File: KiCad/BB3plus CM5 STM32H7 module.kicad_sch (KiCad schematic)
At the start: 9 parts

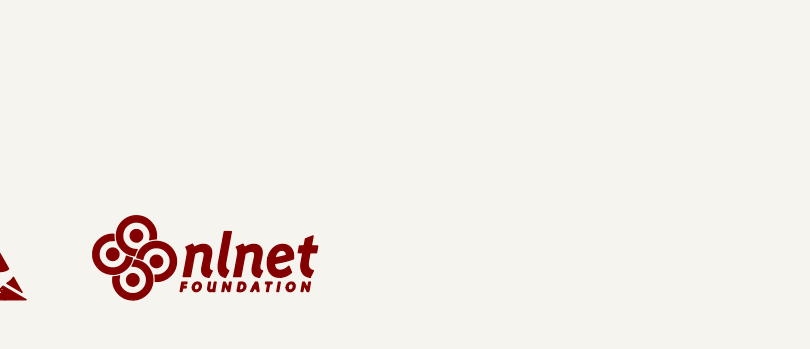
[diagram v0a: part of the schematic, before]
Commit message: USB lanes renamed, OSHWA logo added
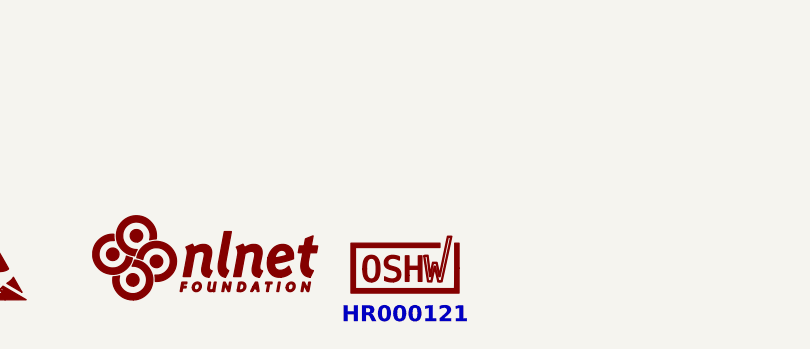
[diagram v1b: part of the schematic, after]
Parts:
- added LOGO6: OSHWA logo, PCM_EEZ_unsorted:OSHWA logo 6.6mm, symbol PCM_EEZ_symbols:OSHWA logo
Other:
- note added: "HR000121"
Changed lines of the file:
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@@
 	(title_block
 		(title "${project_name}")
-		(date "2026-04-09")
+		(date "2026-04-18")
 		(rev "${project_version}")
 		(company "${project_creator}")
@@
 		(comment 2 "${project_info}")
 		(comment 3 "${project_url}")
+	)
+	(text "HR000121"
+		(exclude_from_sim no)
+		(at 90.805 192.405 0)
+		(effects
+			(font
+				(face "DejaVu Sans Mono")
+				(size 1.778 1.778)
+				(bold yes)
+				(color 132 0 0 1)
+			)
+		)
 	)
 	(symbol
@@
 	)
 	(symbol
+		(lib_id "PCM_EEZ_symbols:OSHWA logo")
+		(at 90.805 186.69 0)
+		(unit 1)
+		(body_style 1)
+		(exclude_from_sim no)
+		(in_bom no)
+		(on_board yes)
+		(in_pos_files yes)
+		(dnp no)
+		(fields_autoplaced yes)
+		(property "Reference" "LOGO6"
+			(at 90.805 184.1625 0)
+			(hide yes)
+			(show_name no)
+			(do_not_autoplace no)
+			(effects
+				(font
+					(size 1.27 1.27)
+				)
+			)
+		)
+		(property "Value" "OSHWA logo"
+			(at 90.805 189.2175 0)
+			(hide yes)
+			(show_name no)
+			(do_not_autoplace no)
+			(effects
+				(font
+					(size 1.27 1.27)
+				)
+			)
+		)
+		(property "Footprint" "PCM_EEZ_unsorted:OSHWA logo 6.6mm"
+			(at 90.805 186.69 0)
+			(hide yes)
+			(show_name no)
+			(do_not_autoplace no)
+			(effects
+				(font
+					(size 1.27 1.27)
+				)
+			)
+		)
+		(property "Datasheet" ""
+			(at 90.805 186.69 0)
+			(hide yes)
+			(show_name no)
+			(do_not_autoplace no)
+			(effects
+				(font
+					(size 1.27 1.27)
+				)
+			)
+		)
+		(property "Description" ""
+			(at 90.805 186.69 0)
+			(hide yes)
+			(show_name no)
+			(do_not_autoplace no)
+			(effects
+				(font
+					(size 1.27 1.27)
+				)
+			)
+		)
+		(instances
+			(project "BB3plus CM5 STM32H7 module"
+				(path "/1a4f0aea-3a69-423f-8790-3103cd0321c4"
+					(reference "LOGO6")
+					(unit 1)
+				)
+			)
+		)
+	)
+	(symbol
 		(lib_id "PCM_EEZ_symbols:WEEE logo")
 		(at 38.1 187.96 0)
@@
 		)
 	)
+	(group ""
+		(members "2d837443-f858-499f-8d90-e20a0150e6a6" "45143b85-071f-4e62-8893-099b635e725f")
+	)
 	(sheet

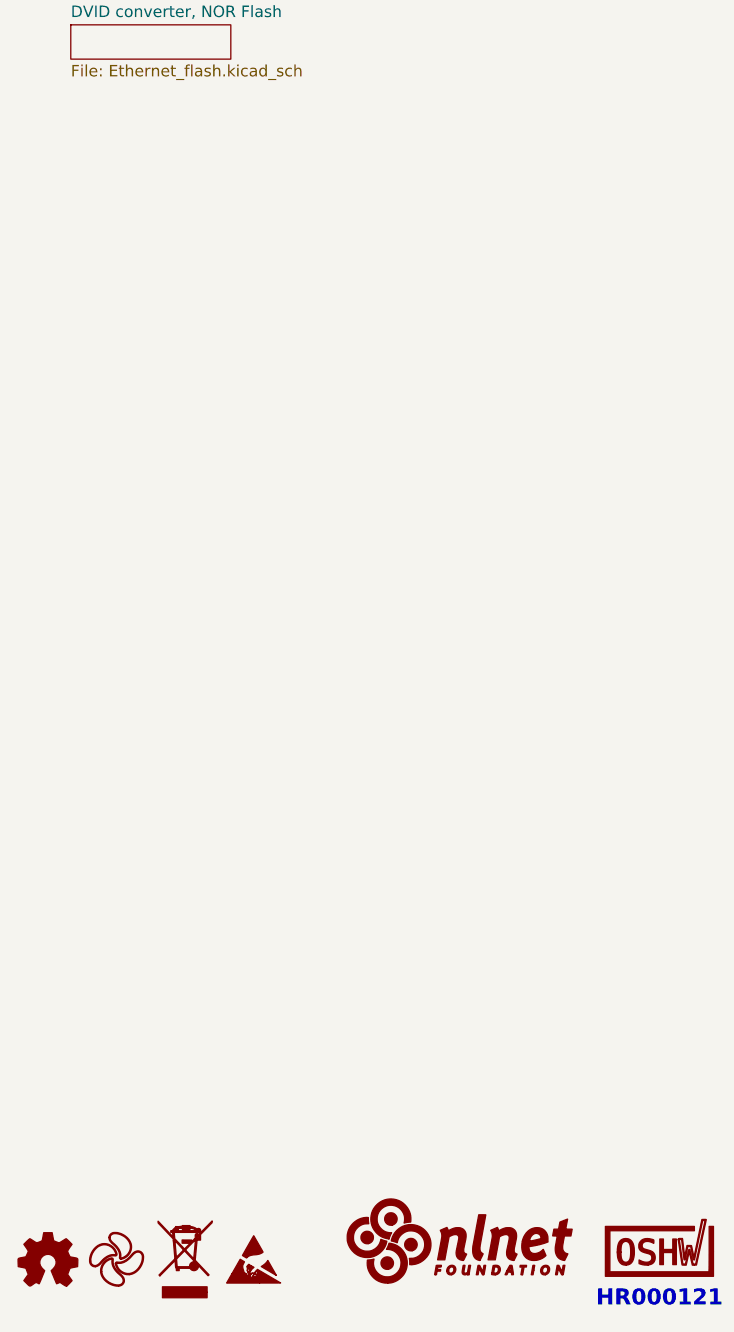
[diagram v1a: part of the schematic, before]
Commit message: Split SoM footprint into two separate 100-pin connectors
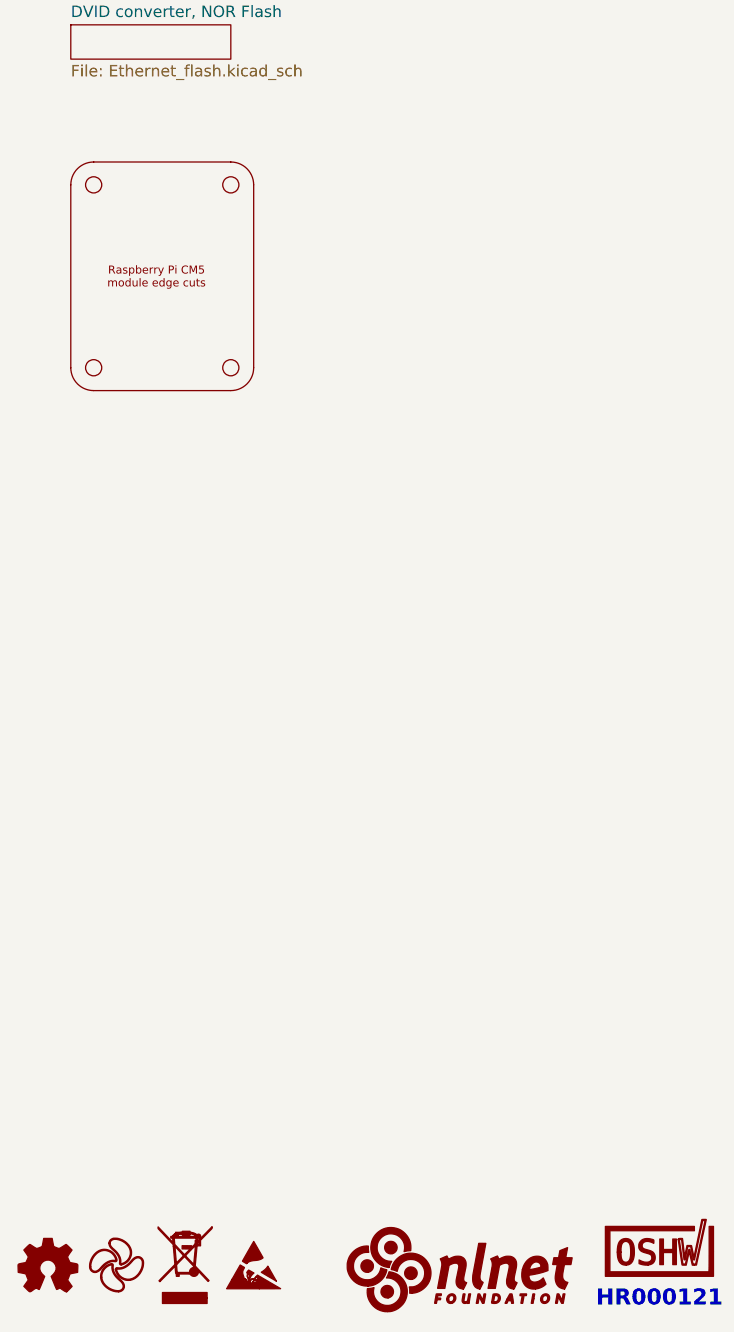
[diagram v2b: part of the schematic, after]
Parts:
- added Module1: (no value), PCM_EEZ_connectors:Raspberry-Pi-CM5 (SoM)_EdgeCuts, symbol PCM_EEZ_connectors:Raspberry Pi CM5 (SoM)_EdgeCuts
- renumbered LOGO2 to LOGO1, LOGO3 to LOGO2, LOGO4 to LOGO3, LOGO5 to LOGO4, LOGO1 to LOGO5
